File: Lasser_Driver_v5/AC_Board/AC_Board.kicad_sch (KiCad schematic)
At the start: 11 parts, among them J1 Screw_Terminal_01x03, J2 Screw_Terminal_01x03, J3 Screw_Terminal_01x03, T1 Triad VPT30-1670, T2 Triad VPT18-8800

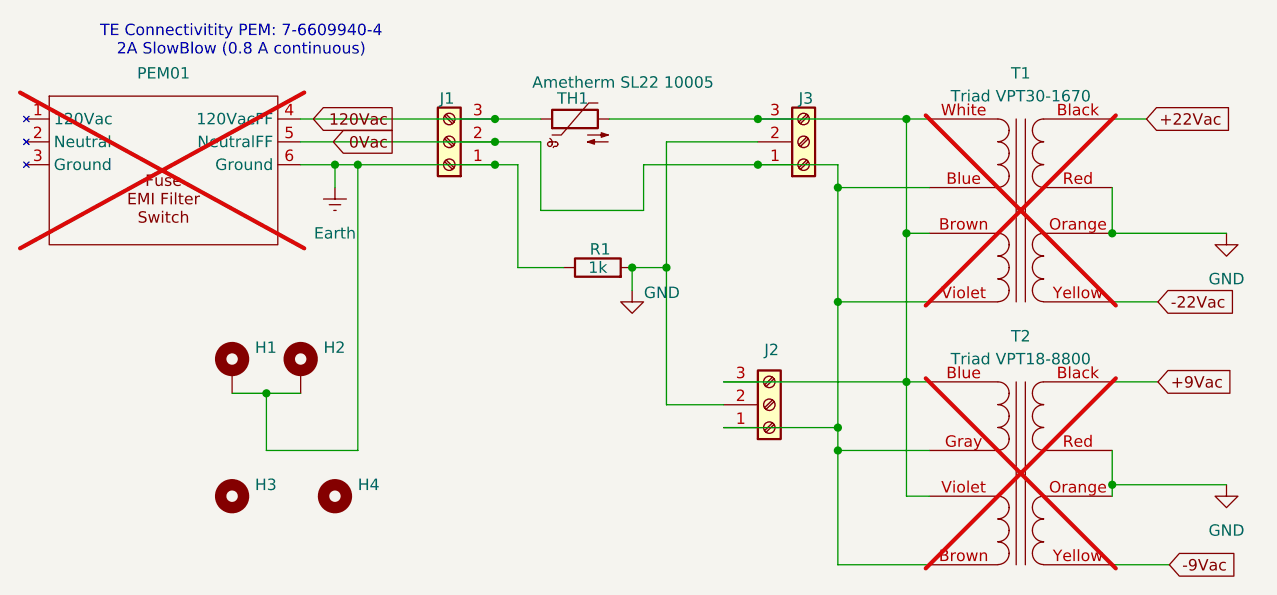
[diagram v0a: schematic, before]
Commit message: v5 ac board and pm22V board ready
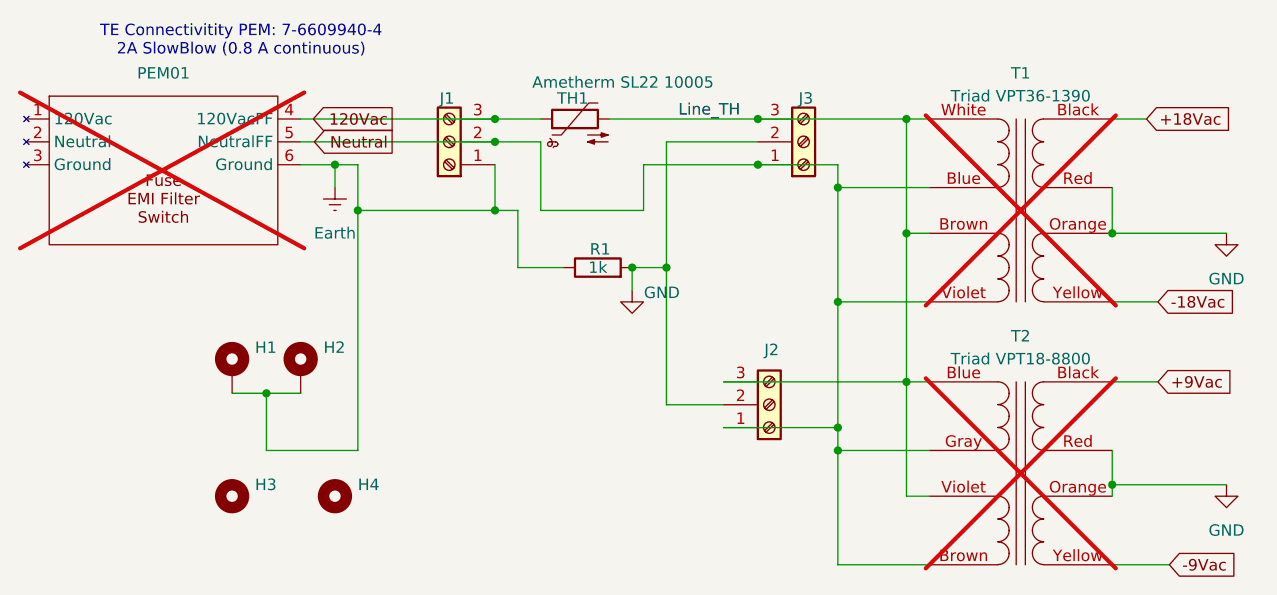
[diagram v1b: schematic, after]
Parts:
- T1: value Triad VPT30-1670 -> Triad VPT36-1390
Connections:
- net Line_TH: now reaches J2.3 (Pin_3), J3.3 (Pin_3), T1.Brown (115V), T1.White (115V), T2.Blue (115V), T2.Violet (115V), TH1.2
- net +22Vac renamed +18Vac
- net -22Vac renamed -18Vac
- net 0Vac renamed Neutral
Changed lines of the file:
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@@
+	)
+	(junction
+		(at 87.63 50.8)
+		(diameter 0)
+		(color 0 0 0 0)
 	)
 	(junction
@@
 	)
 	(junction
-		(at 72.39 45.72)
+		(at 72.39 50.8)
 		(diameter 0)
 		(color 0 0 0 0)
@@
 	)
 	(junction
-		(at 87.63 45.72)
-		(diameter 0)
-		(color 0 0 0 0)
-	)
-	(junction
 		(at 116.84 40.64)
 		(diameter 0)
@@
 	(wire
 		(pts
-			(xy 72.39 77.47) (xy 72.39 45.72)
+			(xy 72.39 77.47) (xy 72.39 50.8)
 		)
 		(stroke
@@
 	(wire
 		(pts
-			(xy 90.17 57.15) (xy 90.17 45.72)
-		)
-		(stroke
-			(width 0)
-			(type default)
-		)
-	)
-	(wire
-		(pts
 			(xy 156.21 77.47) (xy 156.21 81.28)
 		)
@@
 	(wire
 		(pts
+			(xy 87.63 45.72) (xy 87.63 50.8)
+		)
+		(stroke
+			(width 0)
+			(type default)
+		)
+	)
+	(wire
+		(pts
 			(xy 125.73 74.93) (xy 125.73 77.47)
 		)
@@
 	(wire
 		(pts
+			(xy 87.63 50.8) (xy 90.17 50.8)
+		)
+		(stroke
+			(width 0)
+			(type default)
+		)
+	)
+	(wire
+		(pts
 			(xy 116.84 40.64) (xy 133.35 40.64)
 		)
@@
 	(wire
 		(pts
+			(xy 90.17 50.8) (xy 90.17 57.15)
+		)
+		(stroke
+			(width 0)
+			(type default)
+		)
+	)
+	(wire
+		(pts
 			(xy 106.68 43.18) (xy 106.68 57.15)
 		)
@@
 	(wire
 		(pts
+			(xy 72.39 50.8) (xy 87.63 50.8)
+		)
+		(stroke
+			(width 0)
+			(type default)
+		)
+	)
+	(wire
+		(pts
 			(xy 156.21 90.17) (xy 162.56 90.17)
 		)
@@
 	(wire
 		(pts
-			(xy 90.17 45.72) (xy 87.63 45.72)
-		)
-		(stroke
-			(width 0)
-			(type default)
-		)
-	)
-	(wire
-		(pts
 			(xy 156.21 48.26) (xy 156.21 53.34)
 		)
@@
 	(wire
 		(pts
+			(xy 72.39 50.8) (xy 72.39 45.72)
+		)
+		(stroke
+			(width 0)
+			(type default)
+		)
+	)
+	(wire
+		(pts
 			(xy 133.35 53.34) (xy 133.35 82.55)
 		)
@@
 	(wire
 		(pts
-			(xy 72.39 45.72) (xy 87.63 45.72)
-		)
-		(stroke
-			(width 0)
-			(type default)
-		)
-	)
-	(wire
-		(pts
 			(xy 133.35 40.64) (xy 135.89 40.64)
 		)
@@
 			(width 0)
 			(type default)
+		)
+	)
+	(label "Line_TH"
+		(at 108 40.64 0)
+		(effects
+			(font
+				(size 1.27 1.27)
+			)
+			(justify left bottom)
 		)
 	)
@@
 		)
 	)
-	(global_label "-22Vac"
+	(global_label "-18Vac"
 		(shape input)
 		(at 161.29 60.96 0)
@@
 		)
 	)
-	(global_label "0Vac"
+	(global_label "Neutral"
 		(shape output)
 		(at 76.2 43.18 180)
@@
 		)
 		(property "Intersheetrefs" "${INTERSHEET_REFS}"
-			(at 68.6791 43.18 0)
+			(at 66.3206 43.18 0)
 			(hide yes)
 			(show_name no)
@@
 		)
 	)
-	(global_label "+22Vac"
+	(global_label "+18Vac"
 		(shape input)
 		(at 160.02 40.64 0)
@@
 			)
 		)
-		(property "Value" "Triad VPT30-1670"
+		(property "Value" "Triad VPT36-1390"
 			(at 146.05 38.1 0)
 			(show_name no)
